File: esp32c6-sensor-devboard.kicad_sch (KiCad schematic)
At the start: 65 parts, among them J1 Conn_01x04_Pin, J2 Micro_SD_Card_Det1, J3 Screw_Terminal_01x02, J4 USB_C_Receptacle_USB2.0_14P, J5 Screw_Terminal_01x02, SW1 SW_Push, SW2 SW_Push, U1 ESP32-C6, U11 TCA9555RTWR, U2 W25Q128JVS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

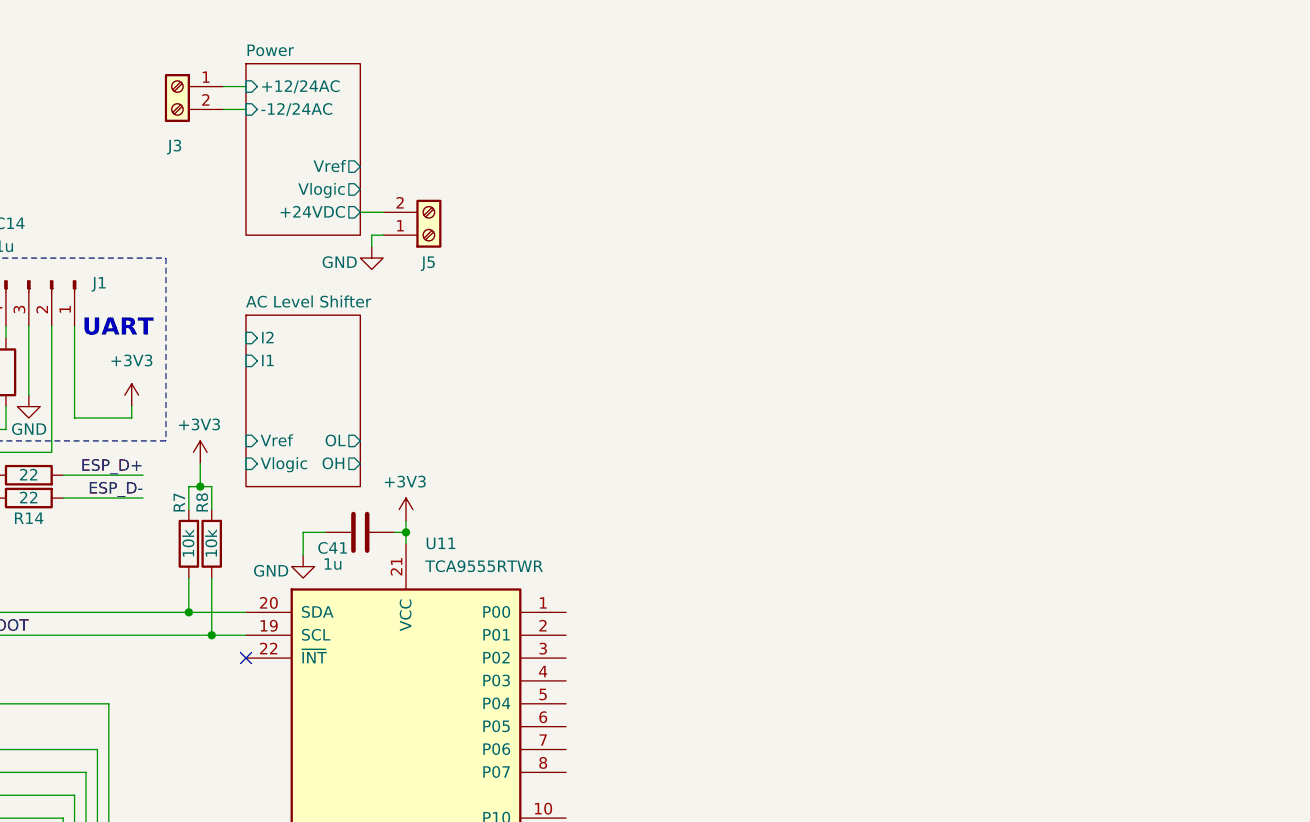
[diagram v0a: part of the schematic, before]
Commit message: schem: add 3CH 24V/12V Input level shifter
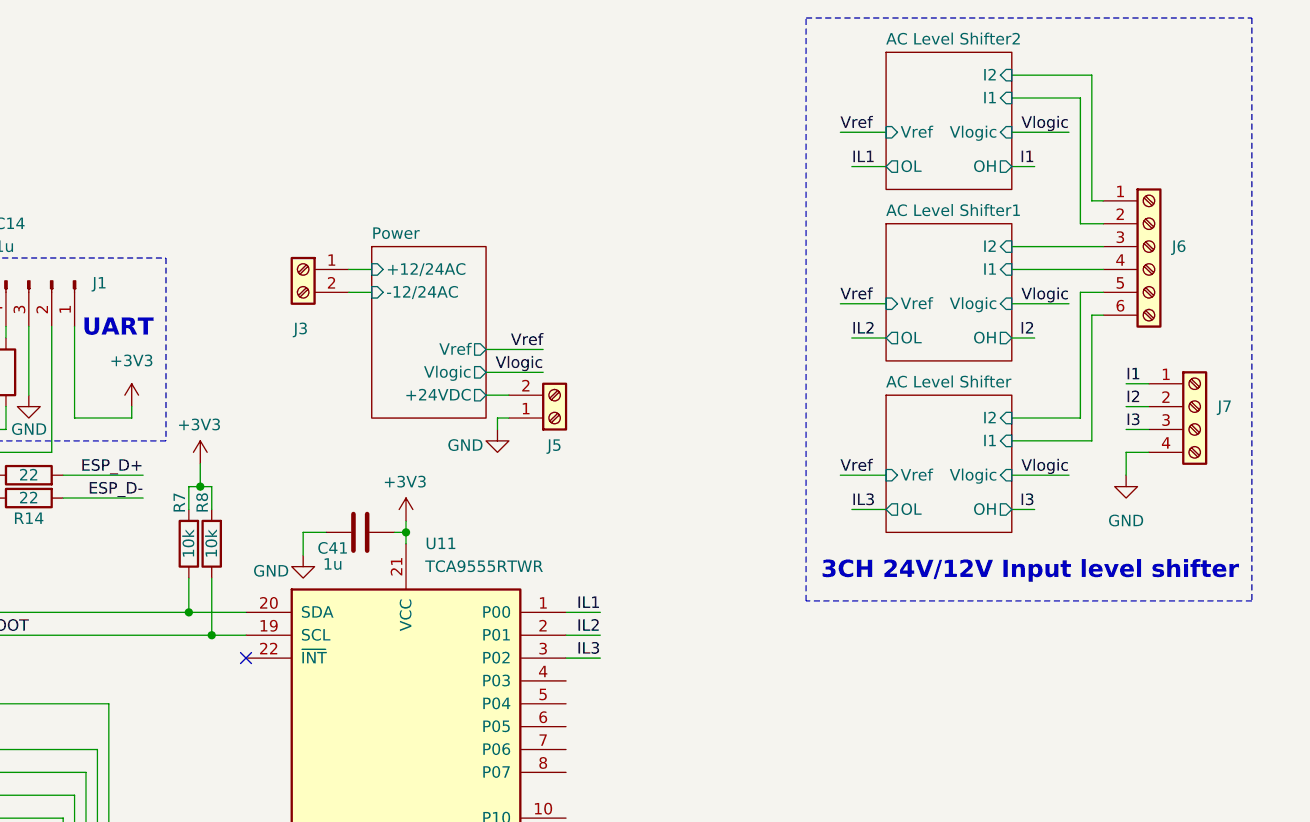
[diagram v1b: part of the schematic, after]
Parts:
- added J6: Screw_Terminal_01x06, symbol Connector:Screw_Terminal_01x06
- added J7: Screw_Terminal_01x04, symbol Connector:Screw_Terminal_01x04
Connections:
- net AC Level Shifter/I1: now also J6.6 (Pin_6)
- net AC Level Shifter/I2: now also J6.5 (Pin_5)
- net GND: now also J7.4 (Pin_4)
- net IL1: now reaches U11.1 (P00)
- net IL2: now reaches U11.2 (P01)
- net IL3: now reaches U11.3 (P02)
- new net AC Level Shifter1/I1: J6.4 (Pin_4)
- new net AC Level Shifter1/I2: J6.3 (Pin_3)
- new net AC Level Shifter2/I1: J6.2 (Pin_2)
- new net AC Level Shifter2/I2: J6.1 (Pin_1)
- new net I1: J7.1 (Pin_1)
- new net I2: J7.2 (Pin_2)
- new net I3: J7.3 (Pin_3)
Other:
- added sheet AC Level Shifter1 (ac-shifter.kicad_sch)
- added sheet AC Level Shifter2 (ac-shifter.kicad_sch)
- note added: "3CH 24V/12V Input level shifter"
- moved on the sheet: J3, J5

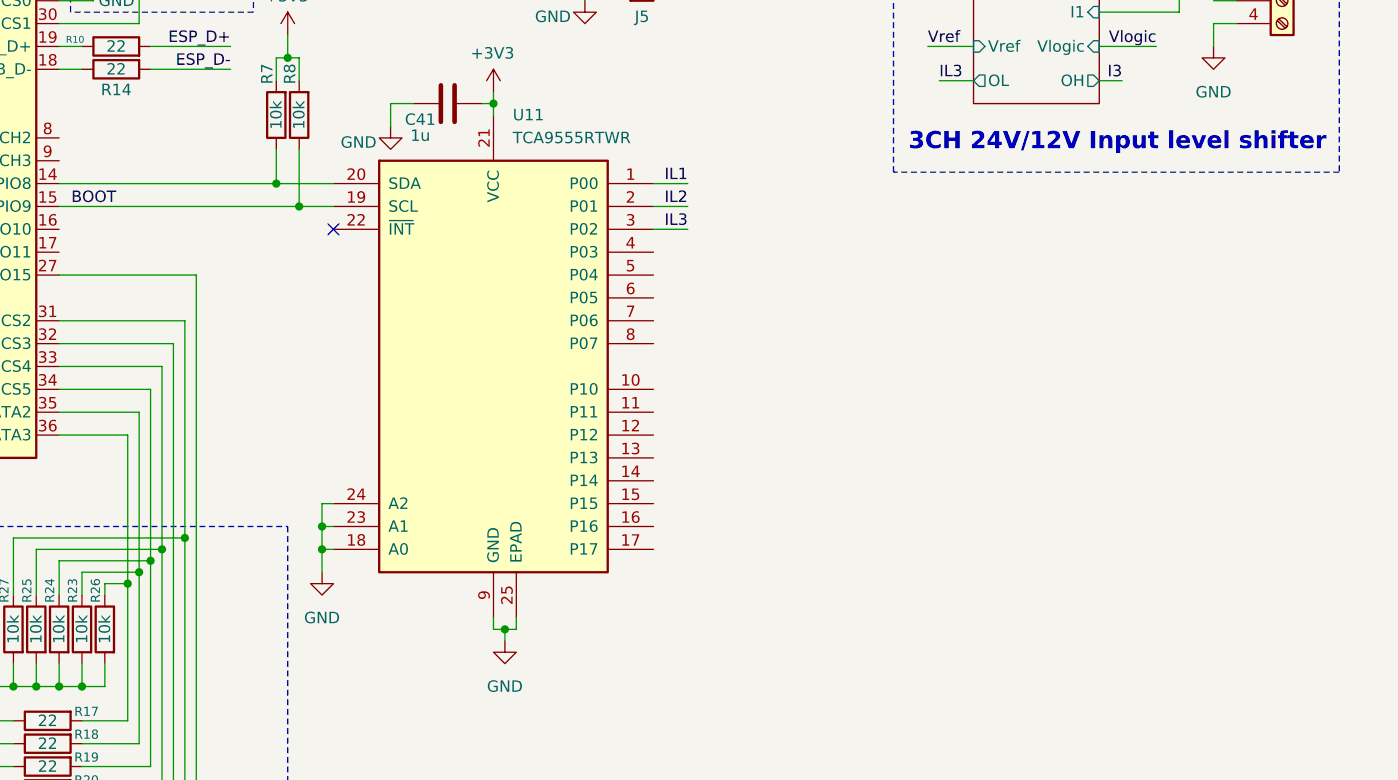
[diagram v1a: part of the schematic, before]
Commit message: schem: add TMP117 temperature sensor
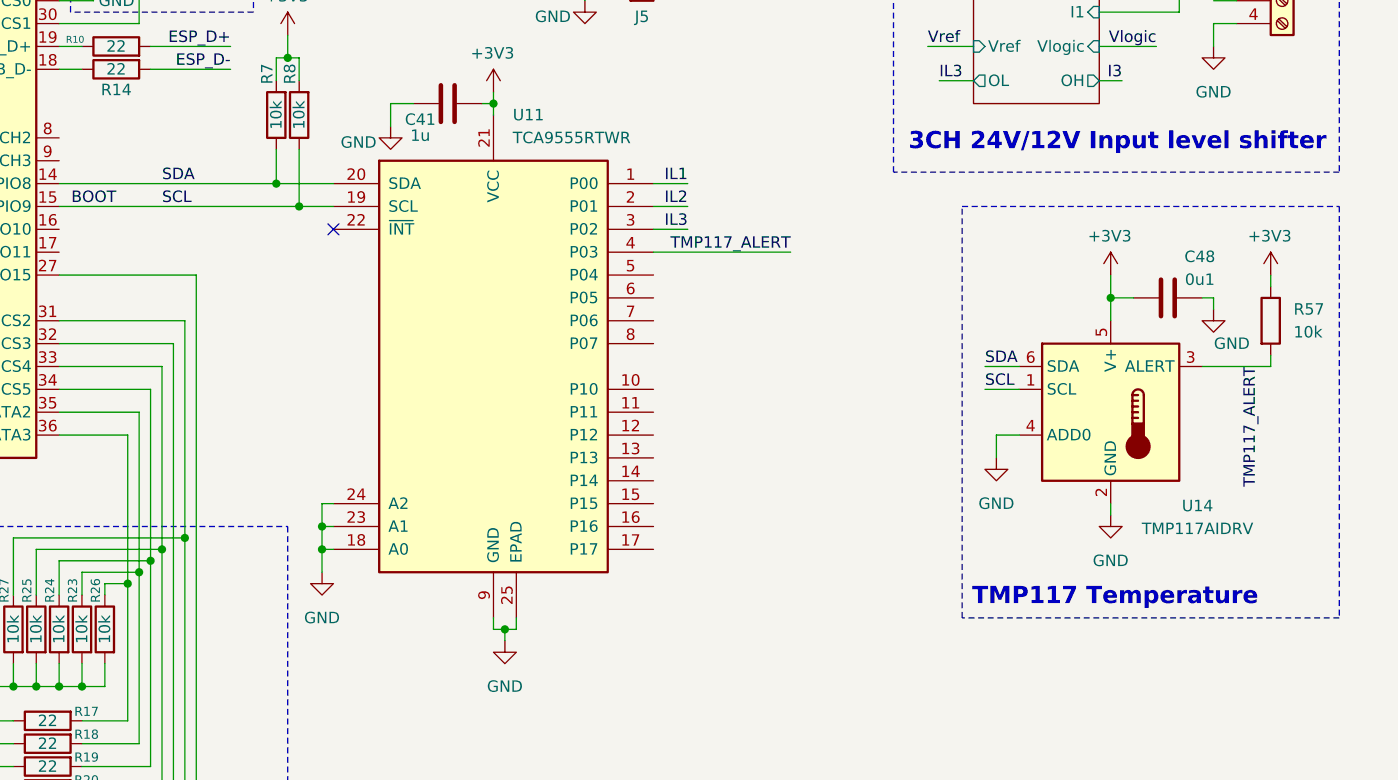
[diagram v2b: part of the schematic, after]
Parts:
- added C48: 0u1, symbol Device:C
- added R57: 10k, symbol Device:R
- added U14: TMP117AIDRV, Package_SON:WSON-6-1EP_2x2mm_P0.65mm_EP1x1.6mm, symbol Sensor_Temperature:TMP117xxDRV
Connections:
- net +3V3: now also C48.1, R57.1, U14.5 (V+)
- net BOOT: now also U14.1 (SCL)
- net GND: now also C48.2, U14.2 (GND), U14.4 (ADD0)
- net SDA: now reaches R7.1, U1.14 (GPIO8), U11.20 (SDA)
- net SDA: now also U14.6 (SDA)
- net TMP117_ALERT: now reaches U11.4 (P03)
- net TMP117_ALERT: now also R57.2, U14.3 (ALERT)
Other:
- note added: "TMP117 Temperature"

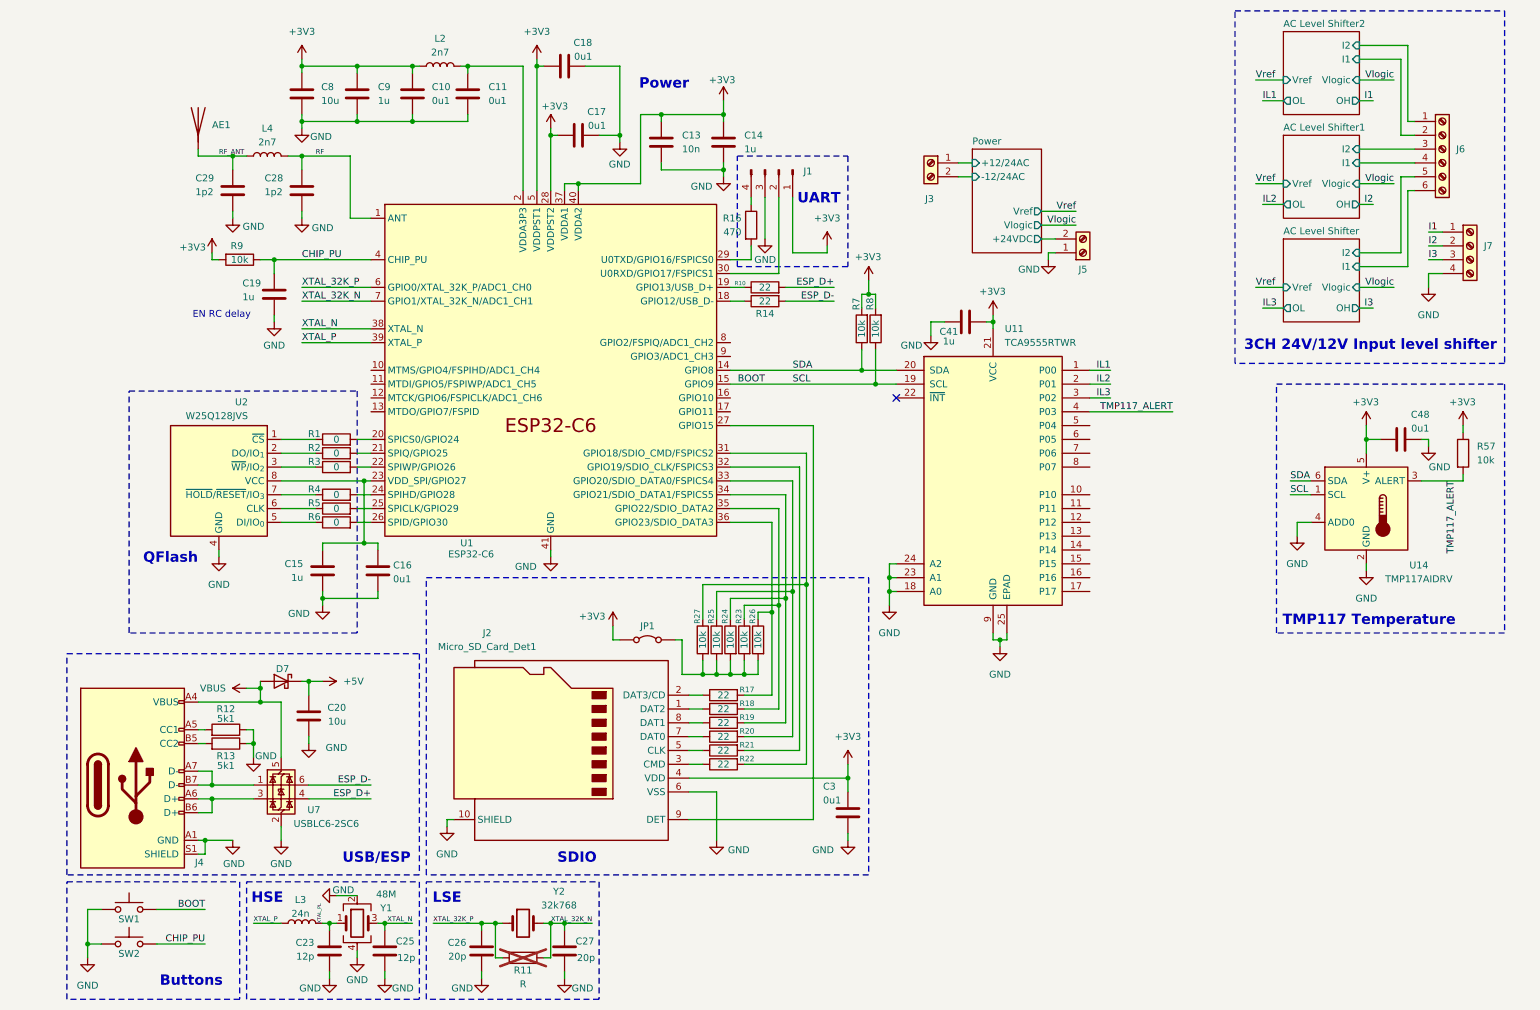
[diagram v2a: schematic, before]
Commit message: schem: add BMP581 I2C pressure sensor
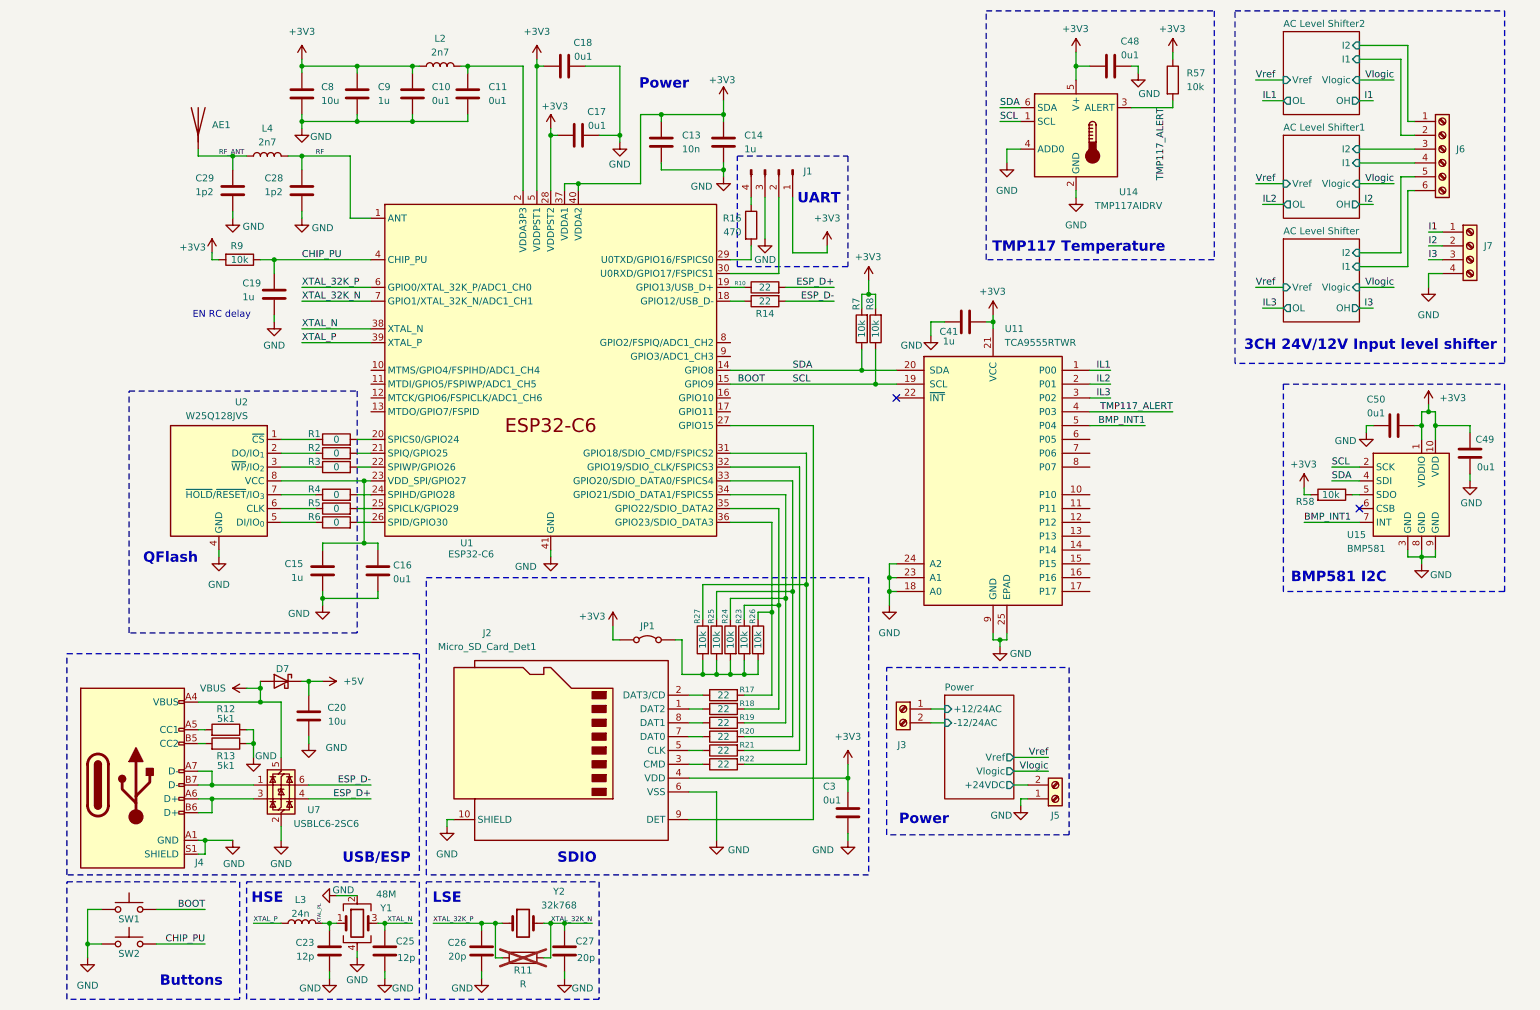
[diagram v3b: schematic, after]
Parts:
- added C49, C50: 0u1, symbol Device:C
- added R58: 10k, symbol Device:R
- added U15: BMP581, Pers:Bosch_LGA-10_2x2mm_P0.8mm_AntiClockwisePinNumbering, symbol Pers:BMP581
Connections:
- net +3V3: now also C49.2, C50.1, R58.2, U15.1 (VDDIO), U15.10 (VDD)
- net BOOT: now also U15.2 (SCK)
- net GND: now also C49.1, C50.2, U15.3 (GND), U15.8 (GND), U15.9 (GND)
- net SDA: now also U15.4 (SDI)
- net BMP_INT1: now reaches U11.5 (P04)
- net BMP_INT1: now also U15.7 (INT)
- new net: R58.1, U15.5 (SDO)
- no-connect marks 1 -> 2
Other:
- note added: "BMP581 I2C"
- moved on the sheet: C48, J3, J5, R57, U14

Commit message: schem: reorganize
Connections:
- net SDA is gone; now on net BOOT: R7.1, U1.14 (GPIO8), U11.20 (SDA), U14.6 (SDA), U15.4 (SDI)
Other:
- moved on the sheet: C15, C16, C41, J3, J5, R1, R2, R3, R4, R5, R6, U11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

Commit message: schem: BMP581 I2C CSB selection
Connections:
- net +3V3: now also U15.6 (CSB)
- no-connect marks 2 -> 1
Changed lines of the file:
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@@
 	)
 	(junction
+		(at 242.57 102.87)
+		(diameter 0)
+		(color 0 0 0 0)
+	)
+	(junction
 		(at 40.64 166.37)
 		(diameter 0)
@@
 		(at 170.18 85.09)
 	)
-	(no_connect
-		(at 252.73 105.41)
-	)
 	(wire
 		(pts
@@
 	(wire
 		(pts
+			(xy 242.57 105.41) (xy 252.73 105.41)
+		)
+		(stroke
+			(width 0)
+			(type default)
+		)
+	)
+	(wire
+		(pts
 			(xy 78.74 24.13) (xy 80.01 24.13)
 		)
@@
 	(wire
 		(pts
+			(xy 242.57 102.87) (xy 242.57 105.41)
+		)
+		(stroke
+			(width 0)
+			(type default)
+		)
+	)
+	(wire
+		(pts
 			(xy 210.82 31.75) (xy 218.44 31.75)
 		)
@@
 		(dnp no)
 		(property "Reference" "R58"
-			(at 241.046 104.14 90)
+			(at 243.586 100.838 90)
 			(effects
 				(font

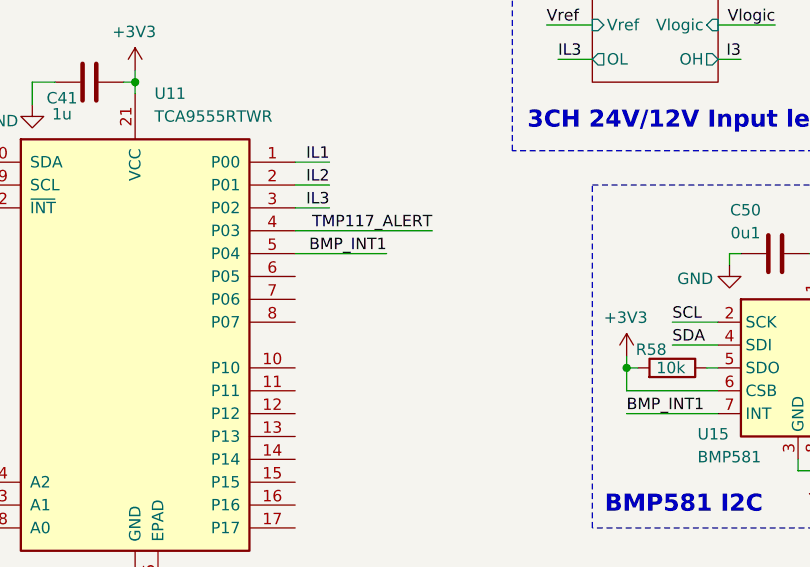
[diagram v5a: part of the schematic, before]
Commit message: schem: add 2 LED indicators
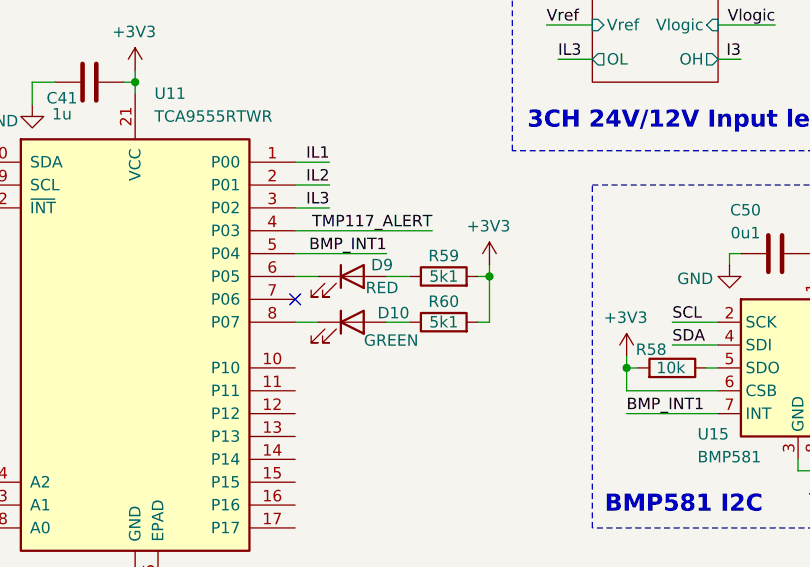
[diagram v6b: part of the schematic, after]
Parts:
- added D10: GREEN, symbol Device:LED
- added D9: RED, symbol Device:LED
- added R59, R60: 5k1, symbol Device:R
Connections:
- net +3V3: now also R59.2, R60.2
- net at U11.6 (P05): now also D9.1 (K)
- net at U11.8 (P07): now also D10.1 (K)
- new net: D10.2 (A), R60.1
- new net: D9.2 (A), R59.1
- no-connect marks 1 -> 2
